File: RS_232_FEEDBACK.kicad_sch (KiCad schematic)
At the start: 48 parts, among them CN1 100nF, CN2 100nF, IC1 MAX11337ATJ+, J26 RS_232, J29 SPARE_ADC, U6 MAX3232CDR

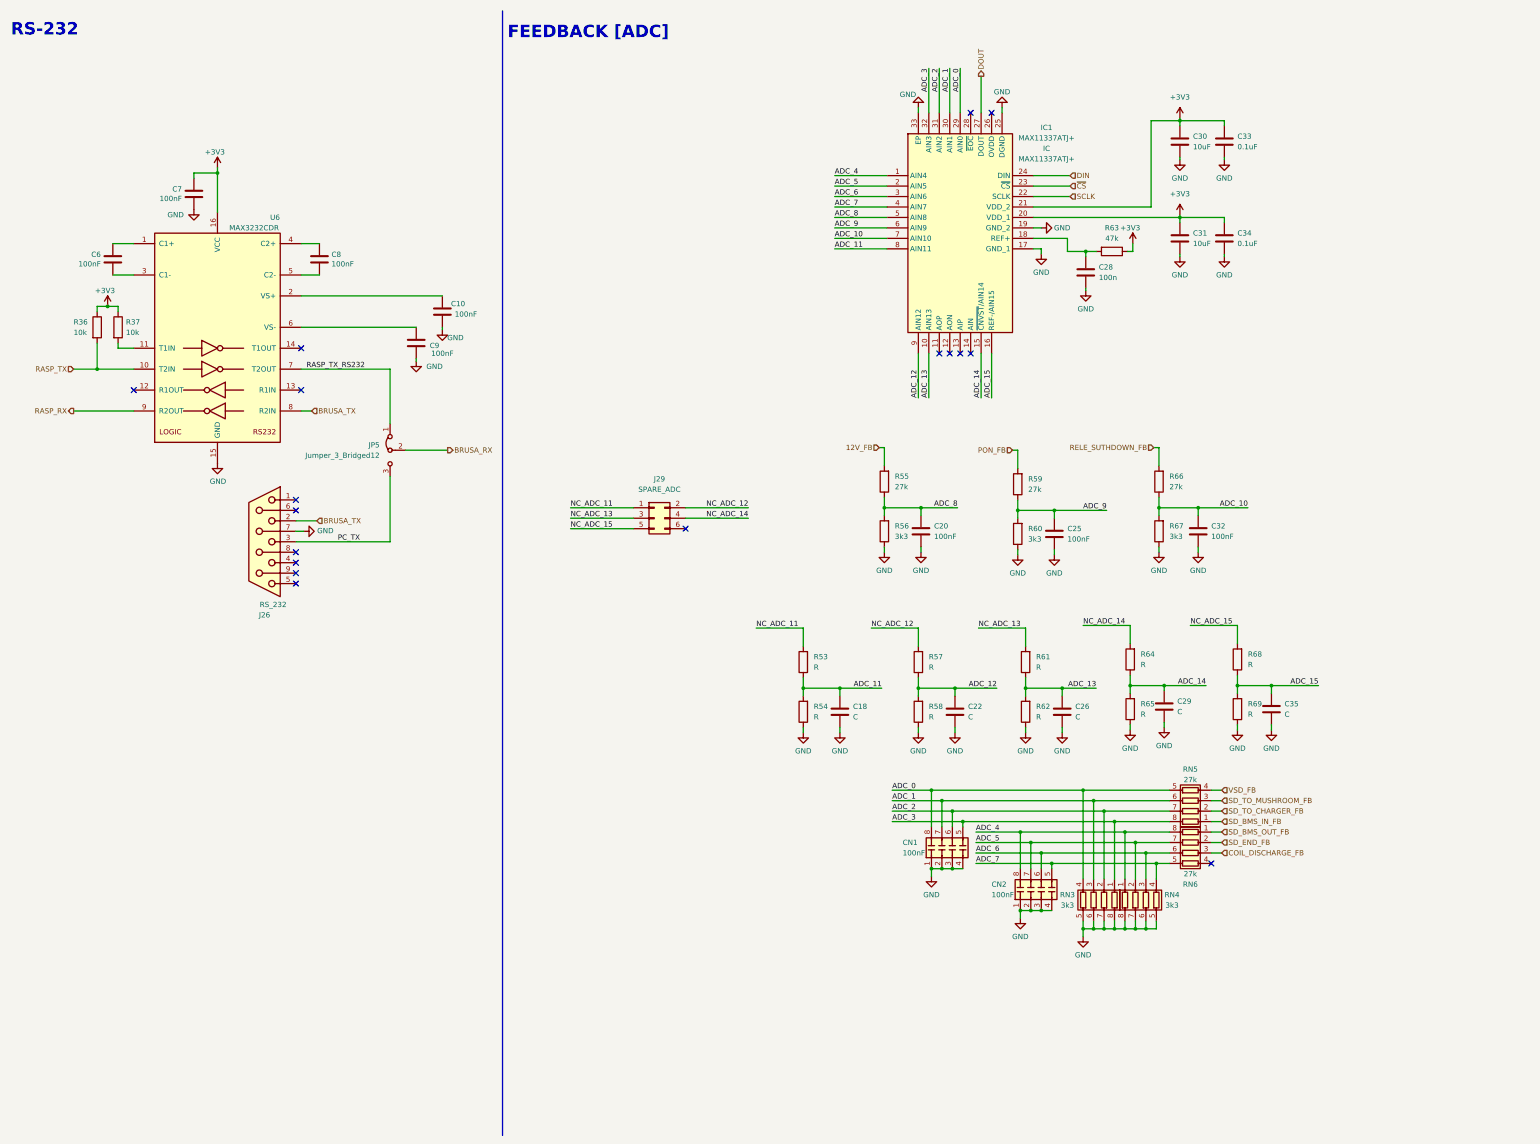
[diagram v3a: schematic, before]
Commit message: Added connector, fixed traces, first version of silkscreen
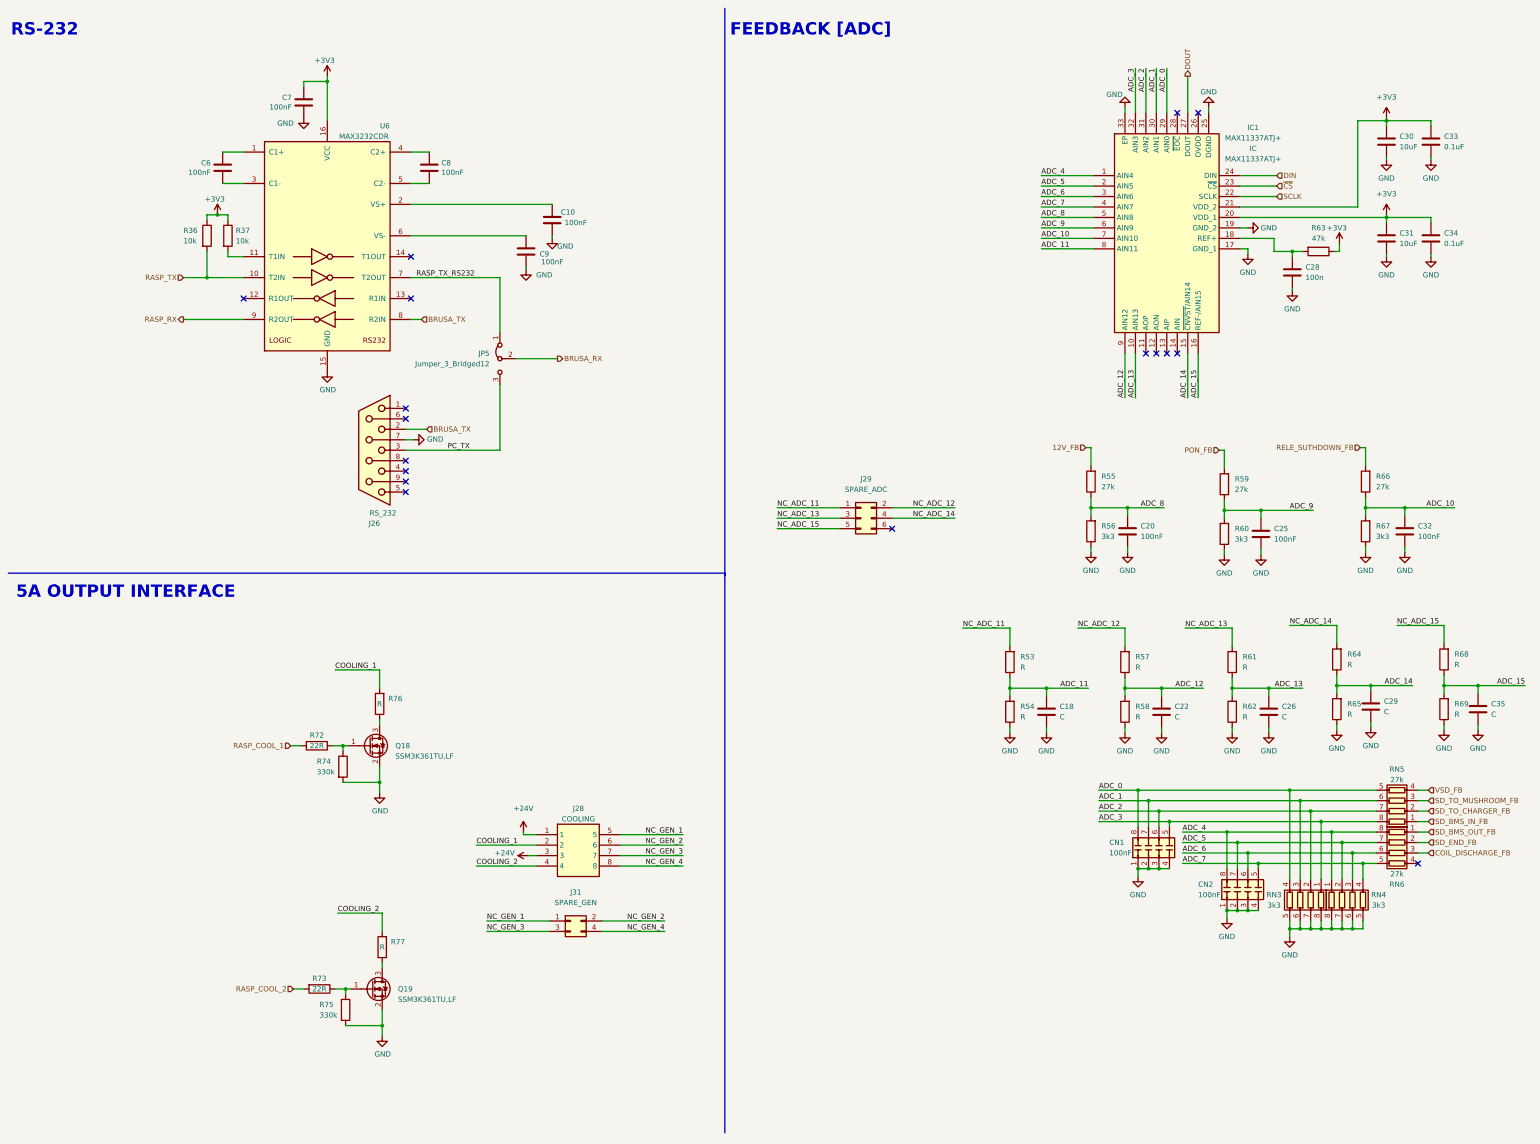
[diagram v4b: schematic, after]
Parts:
- added J28: COOLING, Eagle_Connectors:17762791, symbol 00_proj-lib:1-776279-1
- added J31: SPARE_GEN, Connector_Molex:Molex_Micro-Fit_3.0_43045-0412_2x02_P3.00mm_Vertical, symbol Connector_Generic:Conn_02x02_Odd_Even
- added Q18, Q19: SSM3K361TU,LF, 00_proj-lib:SOTFL65P210X75-3N, symbol Device:Q_NMOS_GSD
- added R72, R73: 22R, Resistor_SMD:R_0603_1608Metric, symbol Device:R
- added R74, R75: 330k, Resistor_SMD:R_0603_1608Metric, symbol Device:R
- added R76, R77: R, Resistor_SMD:R_0805_2012Metric, symbol Device:R
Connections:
- net GND: now also Q18.2 (S), Q19.2 (S), R74.2, R75.2
- new net: Q19.3 (D), R77.1
- new net: Q18.1 (G), R72.1, R74.1
- new net: Q18.3 (D), R76.1
- new net: Q19.1 (G), R73.1, R75.1
- new net +24V: J28.1, J28.3
- new net COOLING_1: J28.2, R76.2
- new net COOLING_2: J28.4, R77.2
- new net NC_GEN_1: J28.5, J31.1 (Pin_1)
- new net NC_GEN_2: J28.6, J31.2 (Pin_2)
- new net NC_GEN_3: J28.7, J31.3 (Pin_3)
- new net NC_GEN_4: J28.8, J31.4 (Pin_4)
- new net RASP_COOL_1: R72.2
- new net RASP_COOL_2: R73.2
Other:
- note added: "5A OUTPUT INTERFACE"
- moved on the sheet: C10, C18, C20, C22, C25, C26, C28, C29, C30, C31, C32, C33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

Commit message: Fixed Schematic, fixed some traces. Still not finished
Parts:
- removed J29: SPARE_ADC, Connector_Molex:Molex_Micro-Fit_3.0_43045-0612_2x03_P3.00mm_Vertical, symbol Connector_Generic:Conn_02x03_Odd_Even
- removed J31: SPARE_GEN, Connector_Molex:Molex_Micro-Fit_3.0_43045-0412_2x02_P3.00mm_Vertical, symbol Connector_Generic:Conn_02x02_Odd_Even
- removed JP5: Jumper_3_Bridged12, Connector_PinHeader_2.54mm:PinHeader_1x03_P2.54mm_Vertical, symbol Jumper:Jumper_3_Bridged12
- removed R37: 10k, Resistor_SMD:R_0603_1608Metric, symbol Device:R
- removed R63: 47k, Resistor_SMD:R_0603_1608Metric, symbol Device:R
- removed U6: MAX3232CDR, Package_SO:SOIC-16_3.9x9.9mm_P1.27mm, symbol Interface_UART:MAX3232
- added C11: 10uF, Capacitor_SMD:C_0805_2012Metric, symbol Device:C
- added C15: 100nF, Capacitor_SMD:C_0603_1608Metric, symbol Device:C
- added J29: SPARE_ADC, Connector_Molex:Molex_Micro-Fit_3.0_43045-0612_2x03_P3.00mm_Vertical, symbol Connector_Generic:Conn_02x03_Top_Bottom
- added J31: SPARE_GEN, Connector_Molex:Molex_Micro-Fit_3.0_43045-0412_2x02_P3.00mm_Vertical, symbol Connector_Generic:Conn_02x02_Top_Bottom
- added JP5: Jumper_3_Bridged12, Connector_PinHeader_2.54mm:PinHeader_1x03_P2.54mm_Vertical, symbol Jumper:Jumper_3_Open
- added JP6: AutoShutdown, Jumper:SolderJumper-3_P1.3mm_Open_RoundedPad1.0x1.5mm, symbol Jumper:SolderJumper_3_Open
- added U6: MAX3221, Package_SO:SSOP-16_4.4x5.2mm_P0.65mm, symbol Interface_UART:MAX3221
- C10, C20, C25, C32, C6, C7, C8, C9: footprint Resistor_SMD:R_0603_1608Metric -> Capacitor_SMD:C_0603_1608Metric
- C18, C22, C26, C29: footprint Resistor_SMD:R_0805_2012Metric -> Capacitor_SMD:C_0805_2012Metric
- C28: value 100n -> 470nF; footprint Resistor_SMD:R_0603_1608Metric -> Capacitor_SMD:C_0805_2012Metric
- C30, C31: footprint Resistor_SMD:R_0603_1608Metric -> Capacitor_SMD:C_0805_2012Metric
- C33, C34: value 0.1uF -> 100nF; footprint Resistor_SMD:R_0603_1608Metric -> Capacitor_SMD:C_0603_1608Metric
- J28: footprint Eagle_Connectors:17762791 -> Eagle_Connectors:TE-17762791
- R53, R54, R57, R58, R61, R62, R64, R65, R68, R69: footprint Resistor_SMD:R_0805_2012Metric -> Resistor_SMD:R_0603_1608Metric
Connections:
- net +3V3: now also C28.1, IC1.18 (REF+), IC1.26 (OVDD), C11.1, C15.1, JP6.1 (A), U6.15 (VCC), U6.16 (~{FORCEOFF})
- net BRUSA_RX: now also JP5.2 (C)
- net BRUSA_TX: now also U6.8 (RIN)
- net GND: now also C11.2, C15.2, J29.6 (Pin_6), JP6.3 (B), U6.1 (~{EN}), U6.14 (GND)
- net NC_ADC_11: now also J29.1 (Pin_1)
- net NC_ADC_12: now also J29.2 (Pin_2)
- net NC_ADC_13: now also J29.3 (Pin_3)
- net NC_ADC_14: now also J29.4 (Pin_4)
- net NC_ADC_15: now also J29.5 (Pin_5)
- net NC_GEN_1: now also J31.1 (Pin_1)
- net NC_GEN_2: now also J31.2 (Pin_2)
- net NC_GEN_3: now also J31.3 (Pin_3)
- net NC_GEN_4: now also J31.4 (Pin_4)
- net PC_TX: now also JP5.3 (B)
- net RASP_RX: now also U6.9 (ROUT)
- net RASP_TX: now also U6.11 (DIN)
- net RASP_TX_RS232: now also JP5.1 (A), U6.13 (DOUT)
- net at IC1.11 (AOP): now also IC1.13 (AIP)
- net at IC1.12 (AON): now also IC1.14 (AIN)
- net at C8.1: now also U6.5 (C2+)
- net at C8.2: now also U6.6 (C2-)
- net at C6.1: now also U6.2 (C1+)
- net at C6.2: now also U6.4 (C1-)
- net at C10.1: now also U6.3 (V+)
- net at C9.1: now also U6.7 (V-)
- net RELE_SUTHDOWN_FB renamed RELAY_SUTHDOWN_FB
- new net: JP6.2 (C), U6.12 (FORCEON)
- no-connect marks 17 -> 9
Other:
- note added: "The old transceiver with 2 channels is in stock, this one is not"
- note added: "The resistance is palced for future need."
- note added: "When the FORCEON pin is drive HIGH the transceiver is Forced ON When the FORCEON pin is drive LOW the tranciever is on AutoShutdown. When no valid signals are present in all the tranciever inputs it turns off until the next valid signal"
- moved on the sheet: C28, C30, C31, C33, C34, CN1, CN2, IC1, RN3, RN4, RN5, RN6

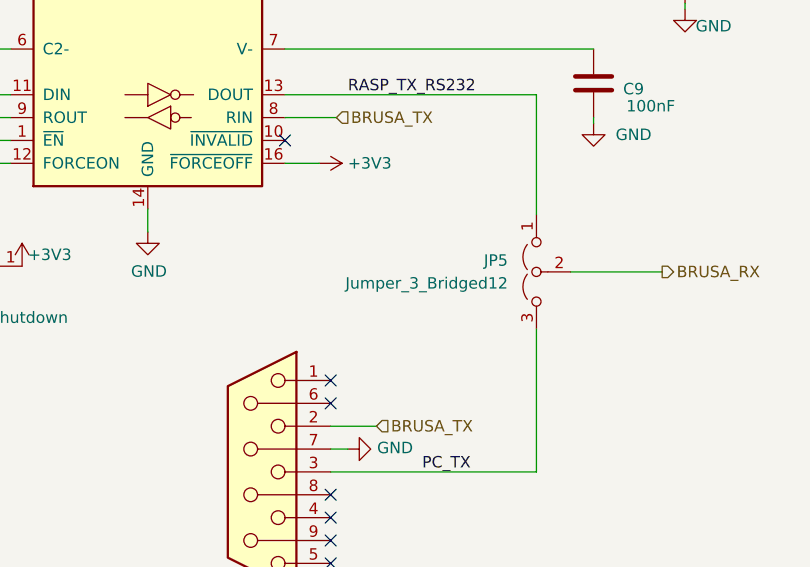
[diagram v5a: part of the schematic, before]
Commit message: Fixed traces, modified silkscreen
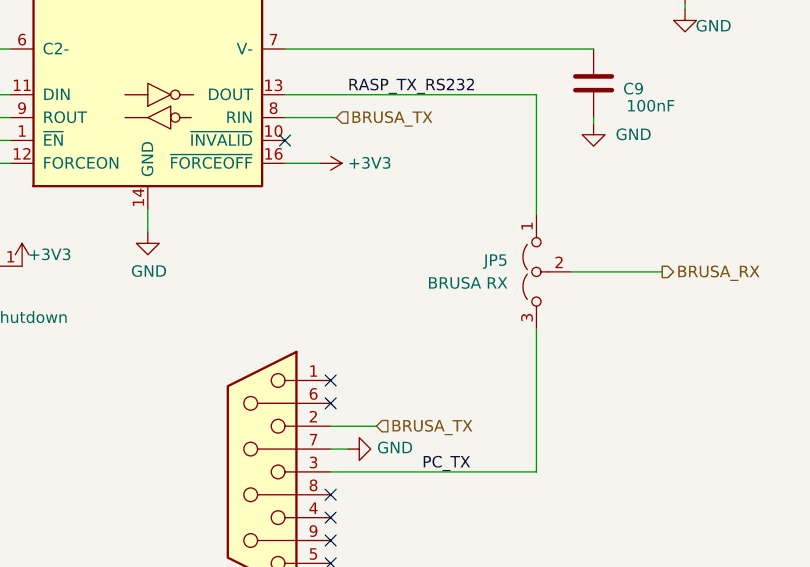
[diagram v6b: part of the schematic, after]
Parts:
- JP5: value Jumper_3_Bridged12 -> BRUSA RX
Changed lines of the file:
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@@
       (effects (font (size 1.27 1.27)) (justify left))
     )
-    (property "Value" "Jumper_3_Bridged12" (id 1) (at 132.08 100.3299 90)
+    (property "Value" "BRUSA RX" (id 1) (at 132.08 100.3299 90)
       (effects (font (size 1.27 1.27)) (justify left))
     )
